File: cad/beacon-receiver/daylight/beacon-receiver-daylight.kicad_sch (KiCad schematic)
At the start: 20 parts, among them J1 STEP-MX02 IF, U1 MCP6022, U2 MCP3201, U3 MCP1525-TT

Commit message: fix(031): daylight KiCad project → own subdir cad/beacon-receiver/daylight/ (KiCad one-project-per-dir; project identity fixed in instances + sheets label; title block added; grid-snapped). v1 sheet untouched. toolchains: synthesized-project lessons
Co-Authored-By: Claude Fable 5 (1M context) <noreply@anthropic.com>
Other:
- title: (none) -> beacon-receiver DAYLIGHT v2 — two-stage AC-coupled (10k TIA -> AC -> U1B x101)
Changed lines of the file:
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@@
 	(generator_version "10.0")
 	(paper "A4")
+	(title_block
+		(title "beacon-receiver DAYLIGHT v2 — two-stage AC-coupled (10k TIA -> AC -> U1B x101)")
+		(date "2026-07-22")
+		(rev "v2-draft")
+		(comment 1 "staged parts at right margin; wire per collector-schematic-daylight.md")
+	)
 	(junction
 		(at 148.59 137.16)
@@
 		)
 		(instances
-			(project "beacon-receiver"
+			(project "beacon-receiver-daylight"
 				(path "/2b38b541-8578-4c8c-87a6-3ec7f952d22b"
 					(reference "U3")
@@
 		)
 		(instances
-			(project "beacon-receiver"
+			(project "beacon-receiver-daylight"
 				(path "/2b38b541-8578-4c8c-87a6-3ec7f952d22b"
 					(reference "R1")
@@
 		)
 		(instances
-			(project "beacon-receiver"
+			(project "beacon-receiver-daylight"
 				(path "/2b38b541-8578-4c8c-87a6-3ec7f952d22b"
 					(reference "U1")
@@
 		)
 		(instances
-			(project "beacon-receiver"
+			(project "beacon-receiver-daylight"
 				(path "/2b38b541-8578-4c8c-87a6-3ec7f952d22b"
 					(reference "C2")
@@
 		)
 		(instances
-			(project "beacon-receiver"
+			(project "beacon-receiver-daylight"
 				(path "/2b38b541-8578-4c8c-87a6-3ec7f952d22b"
 					(reference "C4")
@@
 		)
 		(instances
-			(project "beacon-receiver"
+			(project "beacon-receiver-daylight"
 				(path "/2b38b541-8578-4c8c-87a6-3ec7f952d22b"
 					(reference "PWR1")
@@
 		)
 		(instances
-			(project "beacon-receiver"
+			(project "beacon-receiver-daylight"
 				(path "/2b38b541-8578-4c8c-87a6-3ec7f952d22b"
 					(reference "C3")
@@
 		)
 		(instances
-			(project "beacon-receiver"
+			(project "beacon-receiver-daylight"
 				(path "/2b38b541-8578-4c8c-87a6-3ec7f952d22b"
 					(reference "C1")
@@
 		)
 		(instances
-			(project "beacon-receiver"
+			(project "beacon-receiver-daylight"
 				(path "/2b38b541-8578-4c8c-87a6-3ec7f952d22b"
 					(reference "D1")
@@
 		)
 		(instances
-			(project "beacon-receiver"
+			(project "beacon-receiver-daylight"
 				(path "/2b38b541-8578-4c8c-87a6-3ec7f952d22b"
 					(reference "J1")
@@
 		)
 		(instances
-			(project "beacon-receiver"
+			(project "beacon-receiver-daylight"
 				(path "/2b38b541-8578-4c8c-87a6-3ec7f952d22b"
 					(reference "R2")
@@
 		)
 		(instances
-			(project "beacon-receiver"
+			(project "beacon-receiver-daylight"
 				(path "/2b38b541-8578-4c8c-87a6-3ec7f952d22b"
 					(reference "U1")
@@
 		)
 		(instances
-			(project "beacon-receiver"
+			(project "beacon-receiver-daylight"
 				(path "/2b38b541-8578-4c8c-87a6-3ec7f952d22b"
 					(reference "U1")
@@
 		)
 		(instances
-			(project "beacon-receiver"
+			(project "beacon-receiver-daylight"
 				(path "/2b38b541-8578-4c8c-87a6-3ec7f952d22b"
 					(reference "U2")
@@
 		)
 		(instances
-			(project "beacon-receiver"
+			(project "beacon-receiver-daylight"
 				(path "/2b38b541-8578-4c8c-87a6-3ec7f952d22b"
 					(reference "PWR2")
@@
 		)
 		(instances
-			(project "beacon-receiver"
+			(project "beacon-receiver-daylight"
 				(path "/2b38b541-8578-4c8c-87a6-3ec7f952d22b"
 					(reference "R3")
@@
 		)
 		(instances
-			(project "beacon-receiver"
+			(project "beacon-receiver-daylight"
 				(path "/2b38b541-8578-4c8c-87a6-3ec7f952d22b"
 					(reference "R4")
@@
 		)
 		(instances
-			(project "beacon-receiver"
+			(project "beacon-receiver-daylight"
 				(path "/2b38b541-8578-4c8c-87a6-3ec7f952d22b"
 					(reference "R5")
@@
 		)
 		(instances
-			(project "beacon-receiver"
+			(project "beacon-receiver-daylight"
 				(path "/2b38b541-8578-4c8c-87a6-3ec7f952d22b"
 					(reference "R6")
@@
 		)
 		(instances
-			(project "beacon-receiver"
+			(project "beacon-receiver-daylight"
 				(path "/2b38b541-8578-4c8c-87a6-3ec7f952d22b"
 					(reference "C5")
@@
 		)
 		(instances
-			(project "beacon-receiver"
+			(project "beacon-receiver-daylight"
 				(path "/2b38b541-8578-4c8c-87a6-3ec7f952d22b"
 					(reference "C6")
@@
 		)
 		(instances
-			(project "beacon-receiver"
+			(project "beacon-receiver-daylight"
 				(path "/2b38b541-8578-4c8c-87a6-3ec7f952d22b"
 					(reference "R7")
@@
 		)
 		(instances
-			(project "beacon-receiver"
+			(project "beacon-receiver-daylight"
 				(path "/2b38b541-8578-4c8c-87a6-3ec7f952d22b"
 					(reference "R8")
@@
 		)
 		(instances
-			(project "beacon-receiver"
+			(project "beacon-receiver-daylight"
 				(path "/2b38b541-8578-4c8c-87a6-3ec7f952d22b"
 					(reference "C7")

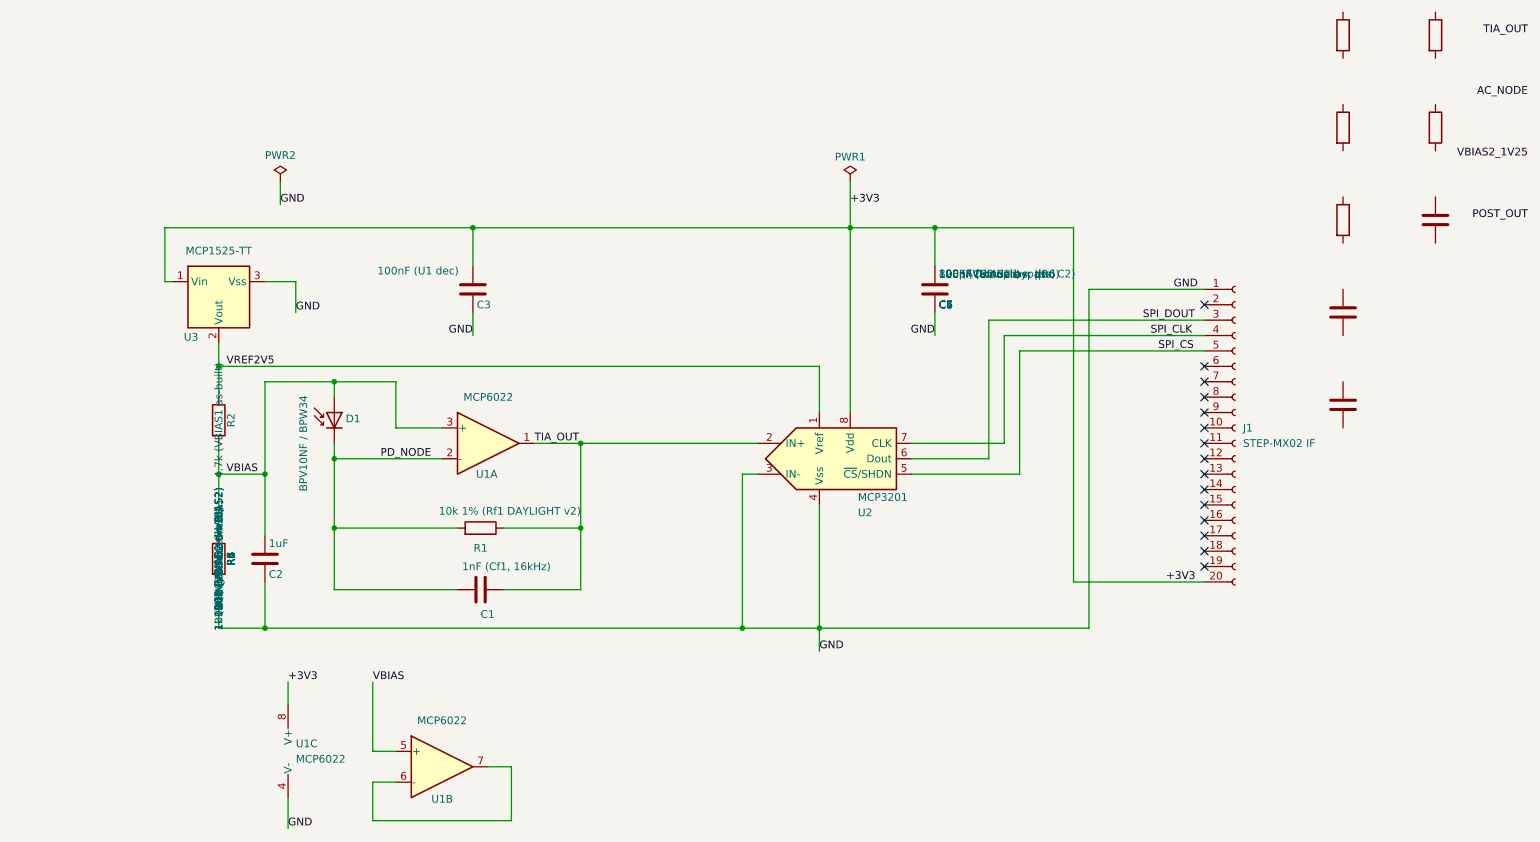
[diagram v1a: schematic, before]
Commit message: feat(031): daylight receiver OPTION C SELECTED — reverse-biased PD + load R + single gain stage (bench-verified close-range + wall-bounce); doc gains netlist/pin-by-pin/DC-transient/SBOA224 cross-check; KiCad sheet revalued [OPT-C] + C8 added (ERC 22 intentional); journal synced for cross-machine pickup
Co-Authored-By: Claude Fable 5 (1M context) <noreply@anthropic.com>
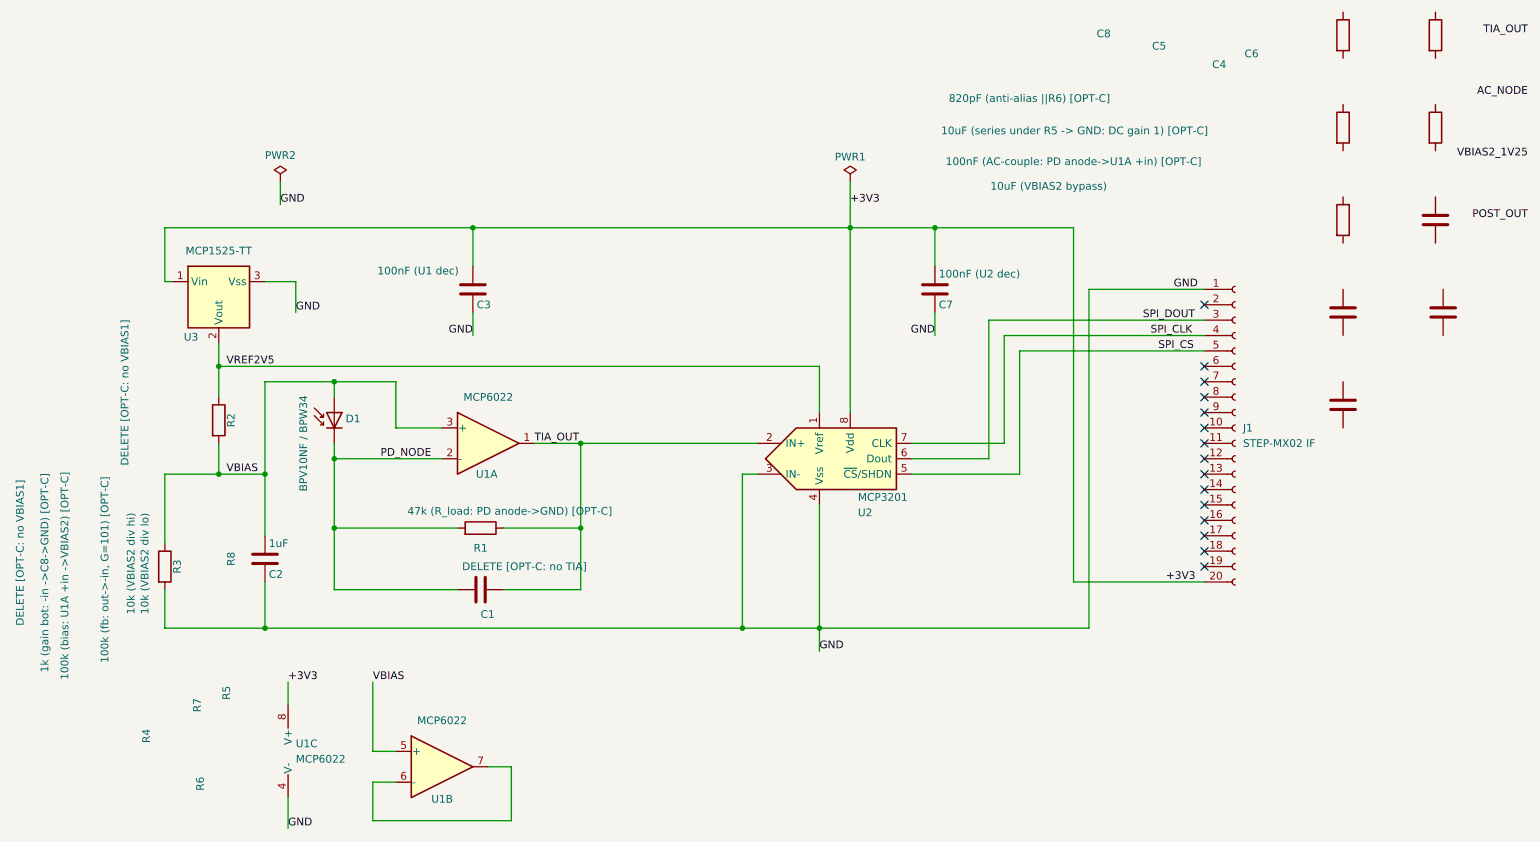
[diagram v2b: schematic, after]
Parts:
- added C8: 10uF (series under R5 -> GND: DC gain 1) [OPT-C], symbol Device:C
- added unit 2 of U1
- C1: value 1nF (Cf1, 16kHz) -> DELETE [OPT-C: no TIA]
- C5: value 820pF (anti-alias, ||R6) -> 820pF (anti-alias ||R6) [OPT-C]
- C6: value 1uF (AC-couple = doc C2) -> 100nF (AC-couple: PD anode->U1A +in) [OPT-C]
- R1: value 10k 1% (Rf1 DAYLIGHT v2) -> 47k (R_load: PD anode->GND) [OPT-C]
- R2: value 4.7k (VBIAS1 as-built) -> DELETE [OPT-C: no VBIAS1]
- R3: value 1k (VBIAS1 as-built) -> DELETE [OPT-C: no VBIAS1]
- R4: value 100k (AC re-bias->VBIAS2) -> 100k (bias: U1A +in ->VBIAS2) [OPT-C]
- R5: value 1k (U1B gain bot->VBIAS2) -> 1k (gain bot: -in ->C8->GND) [OPT-C]
- R6: value 100k (U1B fb, G=101) -> 100k (fb: out->-in, G=101) [OPT-C]
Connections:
- net VBIAS: now also U1.5 (+); no longer U1.5 (+)
- new net: U1.6 (-), U1.7
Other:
- moved on the sheet: R3

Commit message: cad(031): daylight sheet rebuilt to Option C -- wire-level verified, ERC 0
beacon-receiver-daylight.kicad_sch: full Option-C rewire (operator), every
net verified by wire-level walk (MCP query per pin): D1 cathode->3V3 /
anode->PD_NODE, R6 47k load, C6 100n couple, R5 100k bias return, R1 100k
|| C7 820p feedback, R4 2.2k + C5 10u gain leg (x46), R2/R3+C2 VBIAS,
U1B parked, U2 single-ended. ERC 0 (was 22 pre-wiring). D1 = BPW34 by
decision: this sheet is article #2 (lens+filter build, planar PD at the
lens focus); the bare-PD field rig (tests #2/#3) is the BPV10NF.

collector-schematic-daylight.md: refdes renumbered to match the sheet
(doc = sheet = breadboard), netlist table marked wire-level VERIFIED,
gain updated to x46-as-fitted (1k -> x101 option), pin-count audit line,
article-1/article-2 PD split recorded.

Note: en route the file briefly received a v1-sheet edit by mistake --
recovered by copying to the daylight name and reverting beacon-receiver.*.

Co-Authored-By: Claude Fable 5 <noreply@anthropic.com>
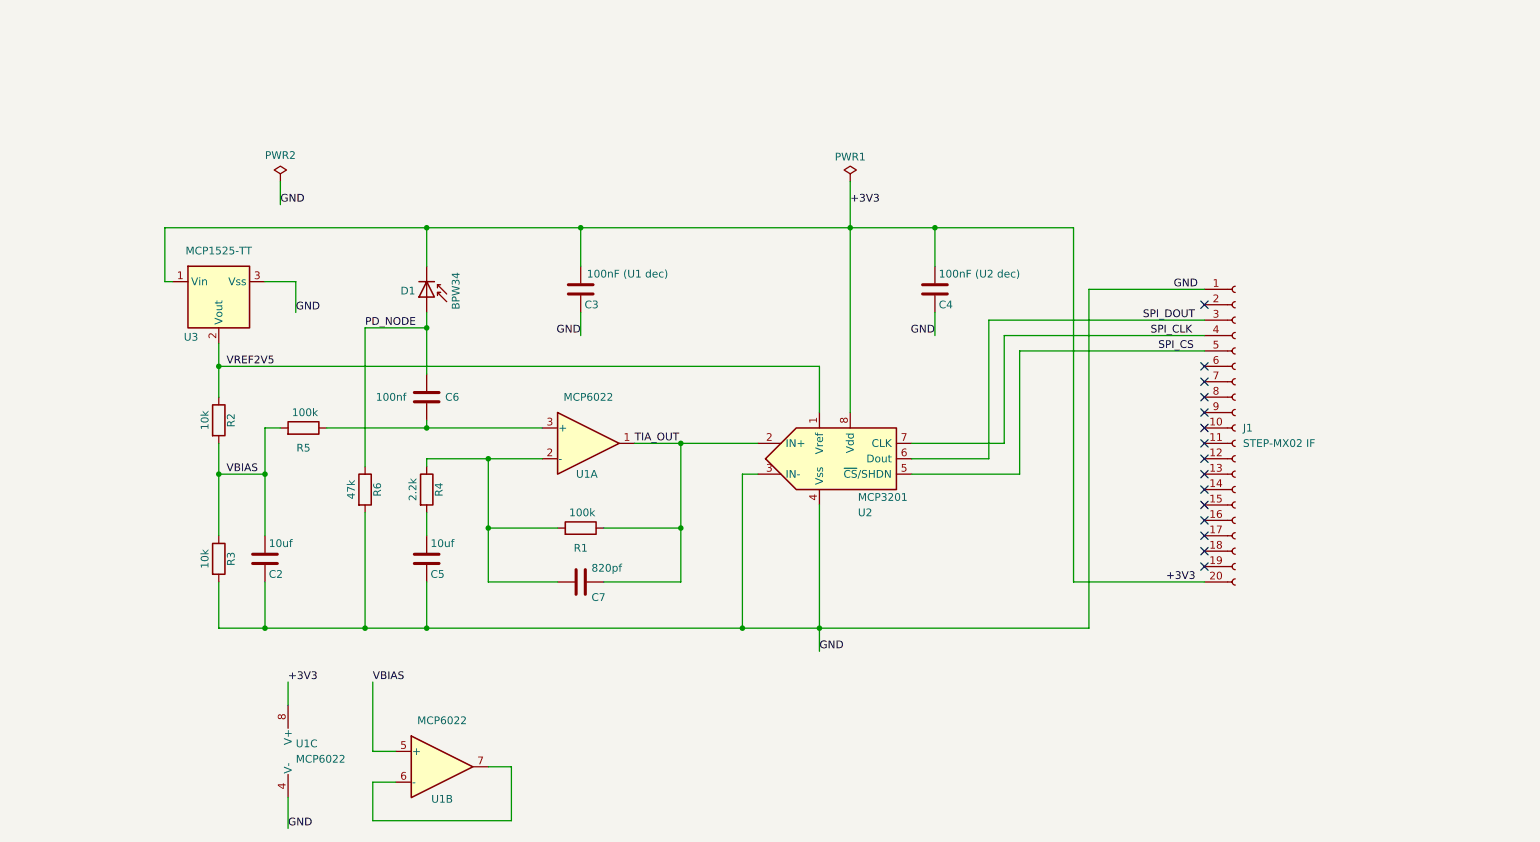
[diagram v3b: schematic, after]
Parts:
- removed C1: DELETE [OPT-C: no TIA], symbol Device:C
- removed C8: 10uF (series under R5 -> GND: DC gain 1) [OPT-C], symbol Device:C
- removed R7: 10k (VBIAS2 div hi), symbol Device:R
- removed R8: 10k (VBIAS2 div lo), symbol Device:R
- C2: value 1uF -> 10uf
- C5: value 820pF (anti-alias ||R6) [OPT-C] -> 10uf
- C6: value 100nF (AC-couple: PD anode->U1A +in) [OPT-C] -> 100nf
- C7: value 10uF (VBIAS2 bypass) -> 820pf
- D1: value BPV10NF / BPW34 -> BPW34
- R1: value 47k (R_load: PD anode->GND) [OPT-C] -> 100k
- R2, R3: value DELETE [OPT-C: no VBIAS1] -> 10k
- R4: value 100k (bias: U1A +in ->VBIAS2) [OPT-C] -> 2.2k
- R5: value 1k (gain bot: -in ->C8->GND) [OPT-C] -> 100k
- R6: value 100k (fb: out->-in, G=101) [OPT-C] -> 47k
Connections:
- net +3V3: now also D1.1 (K)
- net GND: now also C5.2, R6.2
- net PD_NODE: now also C6.1, D1.2 (A), R6.1; no longer D1.1 (K), R1.2, U1.2 (-)
- net TIA_OUT: now also C7.1
- net VBIAS: now also R5.2; no longer D1.2 (A), U1.3 (+)
- net at R4.1: now also C7.2, R1.2, U1.2 (-)
- net at R4.2: now also C5.1
- net at R5.1: now also C6.2, U1.3 (+)
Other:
- title: beacon-receiver DAYLIGHT v2 — two-stage AC-coupled (10k TIA -> AC -> U1B x101) -> (none)
